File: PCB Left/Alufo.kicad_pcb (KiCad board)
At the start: 2 copper layers, 282.6 x 90.9 mm, 95 parts, among them J1 USB_C_Receptacle_USB2.0_16P_2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, J3 USB_C_Receptacle_USB2.0_16P_2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, J5 SolderHole, K11 PG1350, K12 PG1350, K13 PG1350, K14 PG1350, K15 PG1350, K16 PG1350, K21 PG1350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

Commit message: Add cutout in middle layer for solder jump
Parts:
- J5: footprint TestPoint:TestPoint_THTPad_D2.5mm_Drill1.2mm -> Project Library:TestPoint_THTPad_D2.5mm_Drill1.2mm
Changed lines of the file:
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@@
 		)
 	)
-	(footprint "TestPoint:TestPoint_THTPad_D2.5mm_Drill1.2mm"
+	(footprint "Project Library:TestPoint_THTPad_D2.5mm_Drill1.2mm"
 		(layer "F.Cu")
 		(at 238.125 65.166682)
@@
 			)
 		)
-		(property "Footprint" "TestPoint:TestPoint_THTPad_D2.5mm_Drill1.2mm"
+		(property "Footprint" "Project Library:TestPoint_THTPad_D2.5mm_Drill1.2mm"
 			(at 0 0 0)
 			(unlocked yes)
@@
 			(layer "F.CrtYd")
 		)
+		(fp_circle
+			(center 0 0)
+			(end 1.45 0)
+			(stroke
+				(width 0.12)
+				(type solid)
+			)
+			(fill none)
+			(layer "User.2")
+		)
 		(fp_text user "${REFERENCE}"

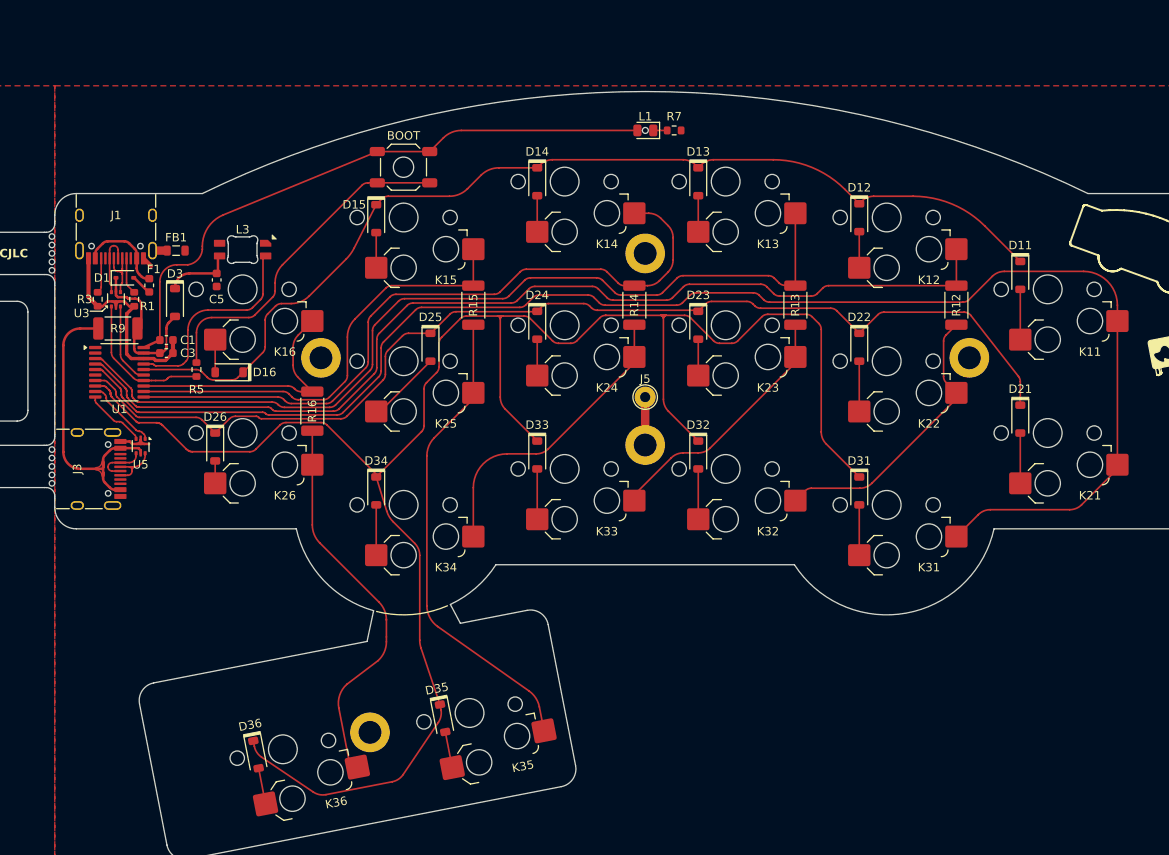
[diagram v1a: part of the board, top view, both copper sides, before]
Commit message: Test direct wiring to an STM32 chip
Sort of works, but there might not be enough room to route all the key connections while keeping good track separation. This would be even worse on the righthand side with the five-way switch!
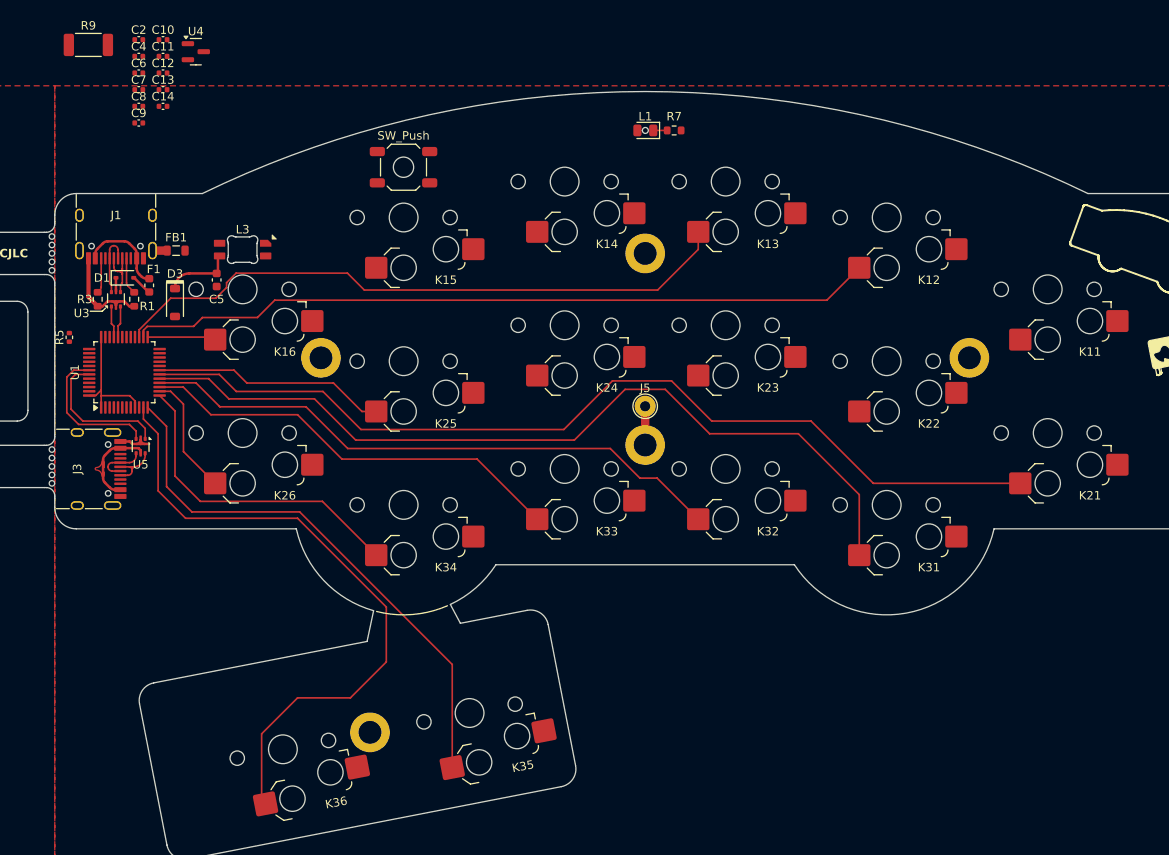
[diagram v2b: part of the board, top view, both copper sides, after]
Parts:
- removed C1, C3: 100nF, Capacitor_SMD:C_0603_1608Metric
- removed D11, D12, D13, D14, D15, D16, D21, D22, D23, D24, D25, D26, D31, D32, D33, D34, D35, D36: 1N4148, Project Library:D_SOD-123_Mod
- removed NT1: NetTie_2, Project Library:NetTie-2_SMD_Pad0.2mm
- removed R12, R13, R14, R15, R16: 0R, Resistor_SMD:R_2010_5025Metric
- added C10: 100nF, Capacitor_SMD:C_0402_1005Metric, F.Cu at (181.1, 22.9)
- added C11: 10nF, Capacitor_SMD:C_0402_1005Metric, F.Cu at (181.1, 24.9)
- added C12: 1uF, Capacitor_SMD:C_0402_1005Metric, F.Cu at (181.1, 26.8)
- added C13: 100nF, Capacitor_SMD:C_0402_1005Metric, F.Cu at (181.1, 28.8)
- added C14: 4.7uF, Capacitor_SMD:C_0402_1005Metric, F.Cu at (181.1, 30.8)
- added C2: 100nF, Capacitor_SMD:C_0402_1005Metric, F.Cu at (178.2, 22.9)
- added C4: 1uF, Capacitor_SMD:C_0402_1005Metric, F.Cu at (178.2, 24.9)
- added C6: 1uF, Capacitor_SMD:C_0402_1005Metric, F.Cu at (178.2, 26.8)
- added C7: 100nF, Capacitor_SMD:C_0402_1005Metric, F.Cu at (178.2, 28.8)
- added C8: 100nF, Capacitor_SMD:C_0402_1005Metric, F.Cu at (178.2, 30.8)
- added C9: 4.7uF, Capacitor_SMD:C_0402_1005Metric, F.Cu at (178.2, 32.7)
- added U4: XC6206, Package_TO_SOT_SMD:SOT-23, F.Cu at (185.0, 24.3)
- R5: value 5k1–20k -> 10k; footprint Resistor_SMD:R_0603_1608Metric -> Resistor_SMD:R_0402_1005Metric
- SW1: value BOOT -> SW_Push
- U1: value CH552T -> STM32F072CBT6; footprint Package_SO:TSSOP-20_4.4x6.5mm_P0.65mm -> Package_QFP:LQFP-48_7x7mm_P0.5mm
- moved R9 33.7 mm to (172.2, 23.5), turned to 0 degrees
- moved R5 15.5 mm to (170.0, 58.1)
- moved J5 1.08 mm to (238.1, 66.2)
- moved U1 0.58 mm to (176.5, 62.2), turned to 90 degrees
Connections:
- D1 pad 1: VCC -> +5V
- D3 pad 2: VCC -> +5V
- J3 pad A6: TX_P -> RX_P
- J3 pad A7: RX_P -> TX_P
- J3 pad B6: TX_P -> RX_P
- J3 pad B7: RX_P -> TX_P
- K11 pad 1: Col1 -> GND
- K11 pad 2: Net-(D11-A) -> K11
- K12 pad 1: Col2 -> GND
- K12 pad 2: Net-(D12-A) -> K12
- K13 pad 1: Col3 -> GND
- K13 pad 2: Net-(D13-A) -> K13
- K14 pad 1: Col4 -> GND
- K14 pad 2: Net-(D14-A) -> K14
- K15 pad 1: Col5 -> GND
- K15 pad 2: Net-(D15-A) -> K15
- K16 pad 1: Col6 -> GND
- K16 pad 2: Net-(D16-A) -> K16
- K21 pad 1: Col1 -> GND
- K21 pad 2: Net-(D21-A) -> K21
- K22 pad 1: Net-(K22-Pad1) -> GND
- K22 pad 2: Net-(D22-A) -> K22
- K23 pad 1: Net-(K23-Pad1) -> GND
- K23 pad 2: Net-(D23-A) -> K23
- K24 pad 1: Net-(K24-Pad1) -> GND
- K24 pad 2: Net-(D24-A) -> K24
- K25 pad 1: Col5T -> GND
- K25 pad 2: Net-(D25-A) -> K25
- K26 pad 1: Col6T -> GND
- K26 pad 2: Net-(D26-A) -> K26
- K31 pad 1: Col1 -> GND
- K31 pad 2: Net-(D31-A) -> K31
- K32 pad 1: Net-(K22-Pad1) -> GND
- K32 pad 2: Net-(D32-A) -> K32
- K33 pad 1: Net-(K23-Pad1) -> GND
- K33 pad 2: Net-(D33-A) -> K33
- K34 pad 1: Net-(K24-Pad1) -> GND
- K34 pad 2: Net-(D34-A) -> K34
- K35 pad 1: Col5T -> GND
- K35 pad 2: Net-(D35-A) -> K35
- K36 pad 1: Col6T -> GND
- K36 pad 2: Net-(D36-A) -> K36
- L1 pad 2: +3V3 -> +3.3V
- R5 pad 1: Net-(NT1-Pad2) -> GND
- R5 pad 2: BOOT -> /BOOT
- R9 pad 1: VCC -> +5V
- SW1 pad 1: BOOT -> +3.3V
- SW1 pad 2: +3V3 -> /BOOT
- U1 pad 1: unconnected-(U1-P3.2-Pad1) -> +3.3V
- U1 pad 10: RX -> unconnected-(U1-PA0-Pad10)
- U1 pad 11: Col4 -> K36
- U1 pad 12: Col5 -> K35
- U1 pad 13: Col6 -> K34
- U1 pad 14: USB+ -> K26
- U1 pad 15: USB- -> K33
- U1 pad 16: Row1 -> K32
- U1 pad 17: LED -> K31
- U1 pad 18: GND -> K21
- U1 pad 19: VCC -> K25
- U1 pad 20: +3V3 -> K23
- U1 pad 3: Col3 -> unconnected-(U1-PC14-Pad3)
- U1 pad 4: Col2 -> unconnected-(U1-PC15-Pad4)
- U1 pad 5: Col1 -> unconnected-(U1-PF0-Pad5)
- U1 pad 7: Row2 -> /NRST
- U1 pad 8: Row3 -> GND
- U1 pad 9: TX -> +3.3V
- U3 pad 5: VCC -> +5V
- U5 pad 1: TX -> RX
- U5 pad 3: RX -> TX
- U5 pad 4: RX_P -> TX_P
- U5 pad 6: TX_P -> RX_P
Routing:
- net Row3: track 222.9 -> 0.00 mm
- net Col1: track 176.4 -> 0.00 mm
- net Row2: track 130.2 -> 0.00 mm
- net Row1: track 122.3 -> 0.00 mm
- net Col2: track 118.8 -> 0.00 mm
- net K21: track 0.00 -> 111.9 mm
- net Col3: track 103.2 -> 0.00 mm
- net K31: track 0.00 -> 100.6 mm
- net K12: track 0.00 -> 88.6 mm
- net Col4: track 82.2 -> 0.00 mm
- net K36: track 0.00 -> 76.5 mm
- net K13: track 0.00 -> 75.0 mm
- net +3V3: track 72.4 -> 0.00 mm
- net K32: track 0.00 -> 70.4 mm
- net K35: track 0.00 -> 65.0 mm
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
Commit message: Add in a few more connections
It really doesn’t look promising!
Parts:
- moved C5 13.0 mm to (184.2, 38.8)
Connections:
- U1 pad 19: K25 -> K24
- U1 pad 20: K23 -> K25
- U1 pad 21: K22 -> K23
- U1 pad 22: K24 -> K22
- U1 pad 26: K12 -> K11
- U1 pad 27: K13 -> K12
- U1 pad 31: K11 -> K13
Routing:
- net K11: track 0.00 -> 108.5 mm
- net K22: track 0.00 -> 93.1 mm
- net K23: track 0.00 -> 67.0 mm
- net K24: track 0.00 -> 50.4 mm
- net K14: track 0.00 -> 43.3 mm
- net K13: track 75.0 -> 48.2 mm
- net LED: track 0.00 -> 20.8 mm
- net Net-(D3-K): track 7.79 -> 0.00 mm
- net K32: track 70.4 -> 72.1 mm
- net K12: track 88.6 -> 90.1 mm
- net K31: track 100.6 -> 102.0 mm
- net K21: track 111.9 -> 113.2 mm

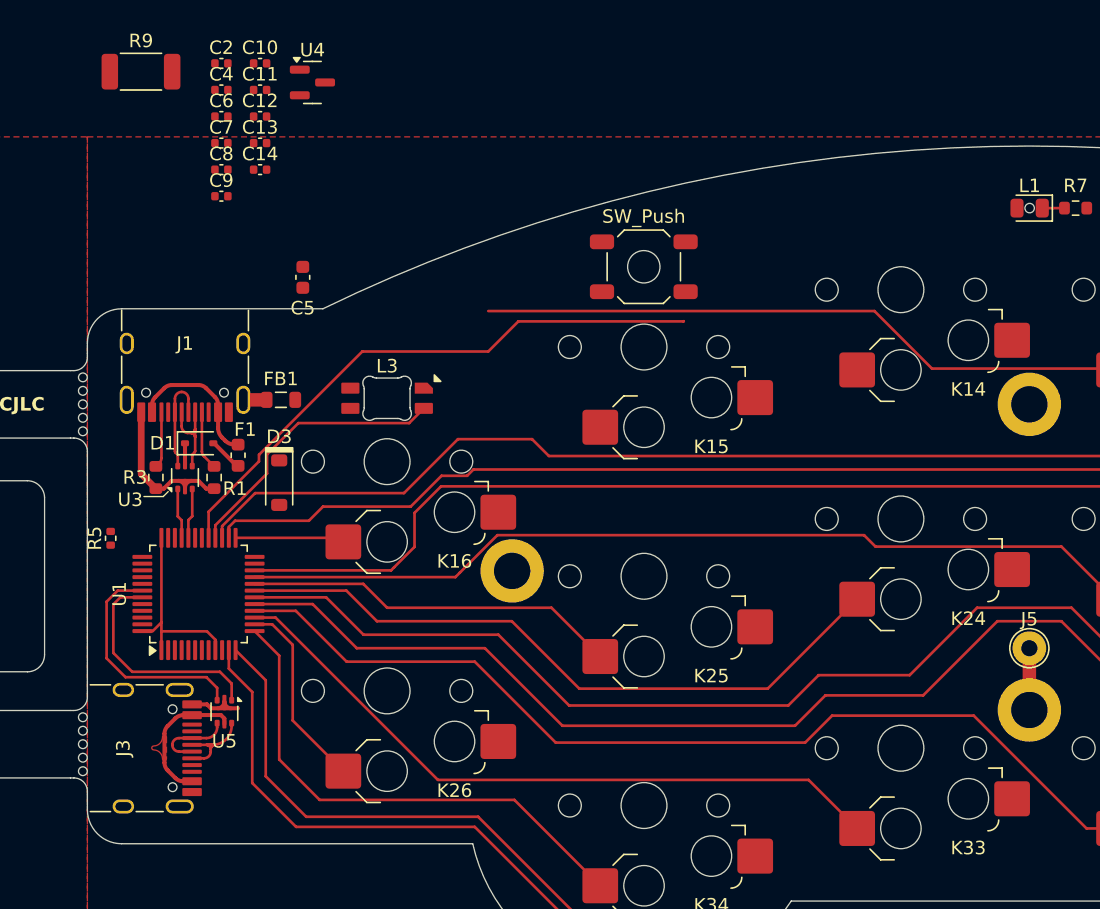
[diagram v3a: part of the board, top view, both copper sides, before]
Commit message: Test routing to STM32F042K6T6
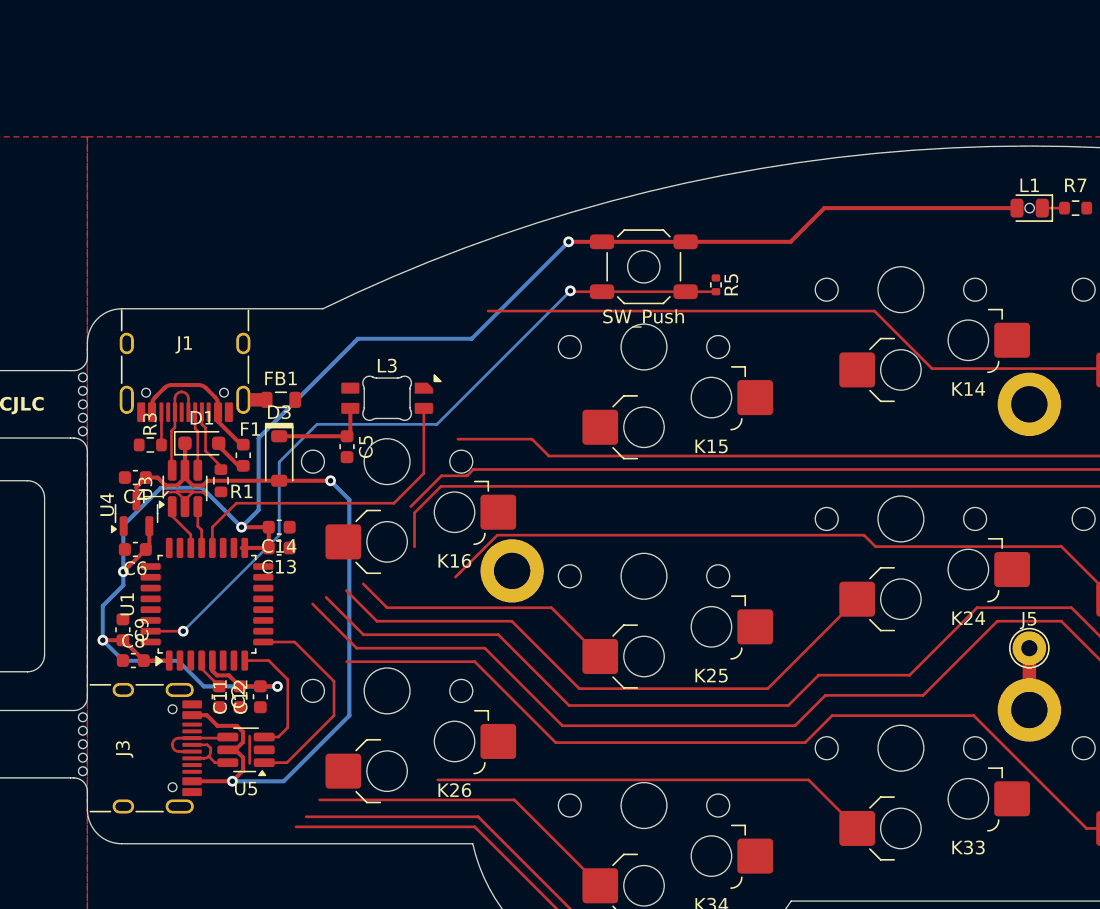
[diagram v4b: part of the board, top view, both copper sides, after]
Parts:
- removed C10, C7: 100nF, Capacitor_SMD:C_0402_1005Metric
- removed R9: 0R, Resistor_SMD:R_2010_5025Metric
- C11, C12, C13, C14, C2, C4, C6, C8, C9: footprint Capacitor_SMD:C_0402_1005Metric -> Capacitor_SMD:C_0603_1608Metric
- D1: footprint Diode_SMD:D_SOD-323 -> Diode_SMD:D_SOD-323_HandSoldering
- U1: footprint Package_QFP:LQFP-48_7x7mm_P0.5mm -> Package_QFP:LQFP-32_7x7mm_P0.8mm
- U3, U5: footprint Project Library:SOT-666_Mod -> Package_TO_SOT_SMD:SOT-23-6_Handsoldering
- moved R5 48.7 mm to (214.9, 39.3), turned to -90 degrees
- moved C2 47.0 mm to (178.1, 69.8), turned to -90 degrees
- moved C11 45.0 mm to (179.6, 69.8), turned to 90 degrees
- moved C12 43.0 mm to (181.1, 69.8), turned to 90 degrees
- moved C8 37.0 mm to (171.7, 67.2)
- moved U4 34.5 mm to (171.9, 56.3), turned to 90 degrees
- moved C9 33.0 mm to (170.9, 64.9), turned to -90 degrees
- moved C6 32.7 mm to (171.8, 58.9), turned to 180 degrees
- moved C13 30.1 mm to (182.5, 58.8), turned to 180 degrees
- moved C4 29.4 mm to (171.8, 53.6), turned to 180 degrees
- moved C14 26.5 mm to (182.5, 57.3), turned to 180 degrees
- moved C5 13.0 mm to (187.5, 51.3)
- moved U5 3.25 mm to (180.0, 73.8), turned to 180 degrees
- moved R3 2.45 mm to (172.9, 51.2), turned to 180 degrees
- moved D3 1.79 mm to (182.5, 52.2)
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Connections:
- J3 pad A4: VCC' -> +5V
- J3 pad A9: VCC' -> +5V
- J3 pad B4: VCC' -> +5V
- J3 pad B9: VCC' -> +5V
- U1 pad 11: K36 -> unconnected-(U1-PA5-Pad11)
- U1 pad 12: K35 -> unconnected-(U1-PA6-Pad12)
- U1 pad 13: K34 -> unconnected-(U1-PA7-Pad13)
- U1 pad 14: K26 -> unconnected-(U1-PB0-Pad14)
- U1 pad 15: K33 -> unconnected-(U1-PB1-Pad15)
- U1 pad 16: K32 -> GND
- U1 pad 17: K31 -> +3.3V
- U1 pad 18: K21 -> unconnected-(U1-PA8-Pad18)
- U1 pad 19: K24 -> unconnected-(U1-PA9-Pad19)
- U1 pad 20: K25 -> LED
- U1 pad 21: K23 -> USB-
- U1 pad 22: K22 -> USB+
- U1 pad 23: GND -> unconnected-(U1-PA13-Pad23)
- U1 pad 24: +3.3V -> unconnected-(U1-PA14-Pad24)
- U1 pad 25: K16 -> unconnected-(U1-PA15-Pad25)
- U1 pad 26: K11 -> unconnected-(U1-PB3-Pad26)
- U1 pad 27: K12 -> unconnected-(U1-PB4-Pad27)
- U1 pad 28: LED -> unconnected-(U1-PB5-Pad28)
- U1 pad 29: K14 -> unconnected-(U1-PB6-Pad29)
- U1 pad 30: K15 -> unconnected-(U1-PB7-Pad30)
- U1 pad 31: K13 -> /BOOT
- U1 pad 32: USB- -> GND
- U1 pad 4: unconnected-(U1-PC15-Pad4) -> /NRST
- U1 pad 5: unconnected-(U1-PF0-Pad5) -> +3.3V
- U1 pad 7: /NRST -> unconnected-(U1-PA1-Pad7)
- U1 pad 8: GND -> TX
- U1 pad 9: +3.3V -> RX
- U5 pad 5: VCC' -> +5V
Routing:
- net +3.3V: track 15.0 -> 126.4 mm, vias 0 -> 5
- net +5V: track 1.61 -> 60.3 mm, vias 0 -> 2
- net /BOOT: track 0.00 -> 55.6 mm, vias 0 -> 2
- net K14: track 43.3 -> 0.00 mm
- net K12: track 90.1 -> 69.1 mm
- net K33: track 51.2 -> 32.6 mm
- net K36: track 76.5 -> 61.4 mm
- net K11: track 108.5 -> 93.6 mm
- net K23: track 67.0 -> 52.1 mm
- net K35: track 65.0 -> 50.5 mm
- net K34: track 38.0 -> 23.4 mm
- net K26: track 14.4 -> 0.00 mm
- net K22: track 93.1 -> 80.5 mm
- net VCC': track 10.5 -> 0.00 mm
- net K32: track 72.1 -> 63.7 mm
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- removed copper zone on F.Cu, net VCC'
